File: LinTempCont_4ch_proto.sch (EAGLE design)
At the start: 76 parts, among them IC1 LM393D, IC3 AD5624R, IC4 AD5262, T1 MMBT3904, T2 MMBT3904, X1 BNC-H, X2 BNC-H

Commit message: Main board progress, started individual channel boards
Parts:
- removed RI, RP: DNP, rlc-jqi:RES0805
- added C16, C17, C18, C19: 10nF, rcl:C-EUC0603
- added C20, C22, C24: 100nF, rlc-jqi:CAP0603
- added C21, C23, C25: 10uF, rlc-jqi:CAP0603
- added D2, D3, D4: (no value), Lin-Temp-Controller:LED/MINI-IND
- added ENC1, ENC2: PEC09, connector-jqi:PEC09
- added IC10, IC5, IC8: AD5262, Lin-Temp-Controller:AD5262
- added IC2, IC7, IC9: LM393D, Lin-Temp-Controller:LM393D
- added JP10, JP12, JP13, JP6, JP7, JP9: (no value), pinhead:PINHD-1X2
- added JP11, JP2, JP8: (no value), pinhead:PINHD-2X6/90
- added R19, R28, R29, R32, R33, R34, R43, R44, R45, R47, R48, R61, R62, R63, R65, R66, R79, R80, R81, R83, R84: 10k, rlc-jqi:RES0603
- added R30, R31, R36: 50, rlc-jqi:RES0603
- added R35: 50, rlc-jqi:RES0805
- added R37, R39, R55, R57, R73, R75: 4.3k, rlc-jqi:RES0603
- added R38, R40, R56, R58, R74, R76: 1.5k, rlc-jqi:RES0603
- added R41, R42, R59, R60, R77, R78: 10k, Lin-Temp-Controller:MODEL64_TRIMPOT/TOP-ADJ
- added R46, R64, R82: 33k, rlc-jqi:RES0603
- added R49, R67, R85: 330, rlc-jqi:RES0603
- added R50, R51, R68, R69, R86, R87: 0, rlc-jqi:RES0603
- added R52, R53, R54, R70, R71, R72, R88, R89, R90: 1.0k, rlc-jqi:RES0603
- added RI1, RI2, RI3, RP1, RP2, RP3: DNP, rlc-jqi:RES0603
- added S2, S3, S4: (no value), Lin-Temp-Controller:SWITCH-DPDT/VER
- added T3, T4, T5, T6, T7, T8: MMBT3904, Lin-Temp-Controller:MMBT3904
- added TP10, TP11, TP12, TP13, TP14, TP15, TP16, TP17, TP18, TP19, TP20, TP21, TP22, TP23, TP24, TP25, TP26, TP9: TESTPT, Lin-Temp-Controller:TESTPT
- added X3, X4, X5, X6, X7, X8: BNC-H, connector-jqi:BNC-H
- C1, C10, C11, C12, C13, C14, C15, C2, C27, C3, C30, C4, C5, C6, C7, C8, C9: device rlc-jqi:CAP0805 -> rlc-jqi:CAP0603
- D1: device Lin-Temp-Controller:LED -> Lin-Temp-Controller:LED/MINI-IND
- L2: device rlc-jqi:INDUCTOR-0805 -> rlc-jqi:INDUCTOR-0603
- R1, R10, R11, R12, R13, R14, R15, R16, R17, R18, R2, R3, R4, R8, R9: device rlc-jqi:RES0805 -> rlc-jqi:RES0603
- R20, R21, R22, R23, R24, R25, R26, R27: device jqi_passives:R_SMDR0805 -> jqi_passives:R_SMDR0603
- R5: value 300 -> 330; device rlc-jqi:RES0805 -> rlc-jqi:RES0603
- S1: device Lin-Temp-Controller:SWITCH-DPDT -> Lin-Temp-Controller:SWITCH-DPDT/VER
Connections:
- net LIMA renamed LIMA1
- net LIMB renamed LIMB1
- removed net +1V: JP1.11, R16.P$2, R17.P$1, RI.P$2, RP.P$1, TP5.P$1
- removed net I: IC4.A2, JP1.12, RI.P$1, TP6.P$1
- removed net N$99: U$1.21/A7/PWM
- removed net P: IC4.A1, JP1.9, RP.P$2, TP4.P$1
- new net +1V_1: JP1.11, R16.P$2, R17.P$1, TP5.P$1
- new net +1V_2: JP2.11, R50.P$2, R51.P$1, RI1.P$2, RP1.P$1, TP12.P$1
- new net +1V_3: JP8.11, R68.P$2, R69.P$1, RI2.P$2, RP2.P$1, TP18.P$1
- new net +1V_4: JP11.11, R86.P$2, R87.P$1, RI3.P$2, RP3.P$1, TP24.P$1
- new net ENC_SW2: ENC2.E, R34.P$1, U$1.21/A7/PWM
- new net I1: IC4.A2, JP1.12, TP6.P$1
- new net I2: IC5.A2, JP2.12, RI1.P$1, TP13.P$1
- new net I3: IC8.A2, JP8.12, RI2.P$1, TP19.P$1
- new net I4: IC10.A2, JP11.12, RI3.P$1, TP25.P$1
- new net LIMA2: JP2.5, R38.P$2, T3.C
- new net LIMA3: JP8.5, R56.P$2, T5.C
- new net LIMA4: JP11.5, R74.P$2, T7.C
- new net LIMB2: JP2.7, R40.P$2, T4.C
- new net LIMB3: JP8.7, R58.P$2, T6.C
- new net LIMB4: JP11.7, R76.P$2, T8.C
- new net N$15: ENC1.GND, R30.P$2
- new net N$16: ENC1.D, R31.P$2
- new net N$17: ENC2.GND, R35.P$2
- new net N$19: ENC2.D, R36.P$2
- new net N$21: JP6.1, R37.P$2, R38.P$1, S2.3
- new net N$22: JP7.1, R39.P$2, R40.P$1, S2.6
- new net N$23: IC2A.-IN, R41.1, R43.P$1, TP9.P$1
- new net N$26: IC2A.OUT, R44.P$1, R45.P$2
- new net N$27: R45.P$1, T3.B
- new net N$28: IC2B.+IN, R42.1, R46.P$1, TP10.P$1
- new net N$29: IC2B.OUT, R47.P$1, R48.P$2
- new net N$30: R48.P$1, T4.B
- new net N$31: D2.C, R49.P$2
- new net N$32: R49.P$1, S2.4
- new net N$33: IC5.B1, IC5.W1, R50.P$1
- new net N$34: IC5.B2, IC5.W2, R51.P$2
- new net N$35: JP2.6, R52.P$1, R53.P$1
- new net N$36: R52.P$2, X3.1
- new net N$37: R54.P$2, X4.1
- new net N$38: JP9.1, R55.P$2, R56.P$1, S3.3
- new net N$39: JP10.1, R57.P$2, R58.P$1, S3.6
- new net N$40: IC7A.-IN, R59.1, R61.P$1, TP15.P$1
- new net N$41: IC7A.OUT, R62.P$1, R63.P$2
- new net N$42: R63.P$1, T5.B
- new net N$43: IC7B.+IN, R60.1, R64.P$1, TP16.P$1
- new net N$44: IC7B.OUT, R65.P$1, R66.P$2
- new net N$45: R66.P$1, T6.B
- new net N$46: D3.C, R67.P$2
- new net N$47: R67.P$1, S3.4
- new net N$48: IC8.B1, IC8.W1, R68.P$1
- new net N$49: IC8.B2, IC8.W2, R69.P$2
- new net N$50: JP8.6, R70.P$1, R71.P$1
- new net N$51: R70.P$2, X5.1
- new net N$52: R72.P$2, X6.1
- new net N$53: JP12.1, R73.P$2, R74.P$1, S4.3
- new net N$54: JP13.1, R75.P$2, R76.P$1, S4.6
- new net N$55: IC9A.-IN, R77.1, R79.P$1, TP21.P$1
- new net N$56: IC9A.OUT, R80.P$1, R81.P$2
- new net N$57: R81.P$1, T7.B
- new net N$58: IC9B.+IN, R78.1, R82.P$1, TP22.P$1
- new net N$59: IC9B.OUT, R83.P$1, R84.P$2
- new net N$60: R84.P$1, T8.B
- new net N$61: D4.C, R85.P$2
- new net N$62: R85.P$1, S4.4
- new net N$63: IC10.B1, IC10.W1, R86.P$1
- new net N$64: IC10.B2, IC10.W2, R87.P$2
- new net N$65: JP11.6, R88.P$1, R89.P$1
- new net N$66: R88.P$2, X7.1
- new net N$67: R90.P$2, X8.1
- new net P1: IC4.A1, JP1.9, TP4.P$1
- new net P2: IC5.A1, JP2.9, RP1.P$2, TP11.P$1
- new net P3: IC8.A1, JP8.9, RP2.P$2, TP17.P$1
- new net P4: IC10.A1, JP11.9, RP3.P$2, TP23.P$1
- net 2.5V: now also JP11.10, JP2.10, JP8.10
- net ACT_T2: now also R53.P$2
- net ACT_T3: now also R71.P$2
- net ACT_T4: now also R89.P$2
- net AGND: now also C20.P$1, C21.P$1, C22.P$1, C23.P$1, C24.P$1, C25.P$1, IC10.GND, IC2P.V-, IC5.GND, IC7P.V-, IC8.GND, IC9P.V-, JP10.2, JP11.2, JP12.2, JP13.2, JP2.2, JP6.2, JP7.2, JP8.2, JP9.2, R37.P$1, R39.P$1, R41.2, R41.3, R42.2, R42.3, R55.P$1, R57.P$1, R59.2, R59.3, R60.2, R60.3, R73.P$1, R75.P$1, R77.2, R77.3, R78.2, R78.3, S2.2, S2.5, S3.2, S3.5, S4.2, S4.5, T3.E, T4.E, T5.E, T6.E, T7.E, T8.E, X3.2, X4.2, X5.2, X6.2, X7.2, X8.2
- net CS_POT2: now also IC5.CS
- net CS_POT3: now also IC8.CS
- net CS_POT4: now also IC10.CS
- net DGND: now also C16.1, C17.1, C18.1, C19.1, IC10.VSS, IC5.VSS, IC8.VSS, R30.P$1, R31.P$1, R35.P$1, R36.P$1
- net ENC_A1: now also C17.2, ENC1.A, R28.P$1
- net ENC_A2: now also C19.2, ENC2.A, R33.P$1
- net ENC_B1: now also C16.2, ENC1.B, R19.P$1
- net ENC_B2: now also C18.2, ENC2.B, R32.P$1
- net ENC_SW1: now also ENC1.E, R29.P$1
- net MOSI_B: now also IC10.SDI, IC5.SDI, IC8.SDI
- net SCK_B: now also IC10.CLK, IC5.CLK, IC8.CLK
- net VDD: now also C20.P$2, C21.P$2, C22.P$2, C23.P$2, C24.P$2, C25.P$2, D2.A, D3.A, D4.A, IC10.PR, IC10.SHDN, IC10.VDD, IC10.VL, IC2P.V+, IC5.PR, IC5.SHDN, IC5.VDD, IC5.VL, IC7P.V+, IC8.PR, IC8.SHDN, IC8.VDD, IC8.VL, IC9P.V+, JP11.1, JP2.1, JP8.1, R19.P$2, R28.P$2, R29.P$2, R32.P$2, R33.P$2, R34.P$2, R43.P$2, R44.P$2, R46.P$2, R47.P$2, R61.P$2, R62.P$2, R64.P$2, R65.P$2, R79.P$2, R80.P$2, R82.P$2, R83.P$2
- net VMON2: now also JP2.8, R54.P$1
- net VMON3: now also JP8.8, R72.P$1
- net VMON4: now also JP11.8, R90.P$1
- net VSET2: now also IC2A.+IN, IC2B.-IN, JP2.3, TP14.P$1
- net VSET3: now also IC7A.+IN, IC7B.-IN, JP8.3, TP20.P$1
- net VSET4: now also IC9A.+IN, IC9B.-IN, JP11.3, TP26.P$1

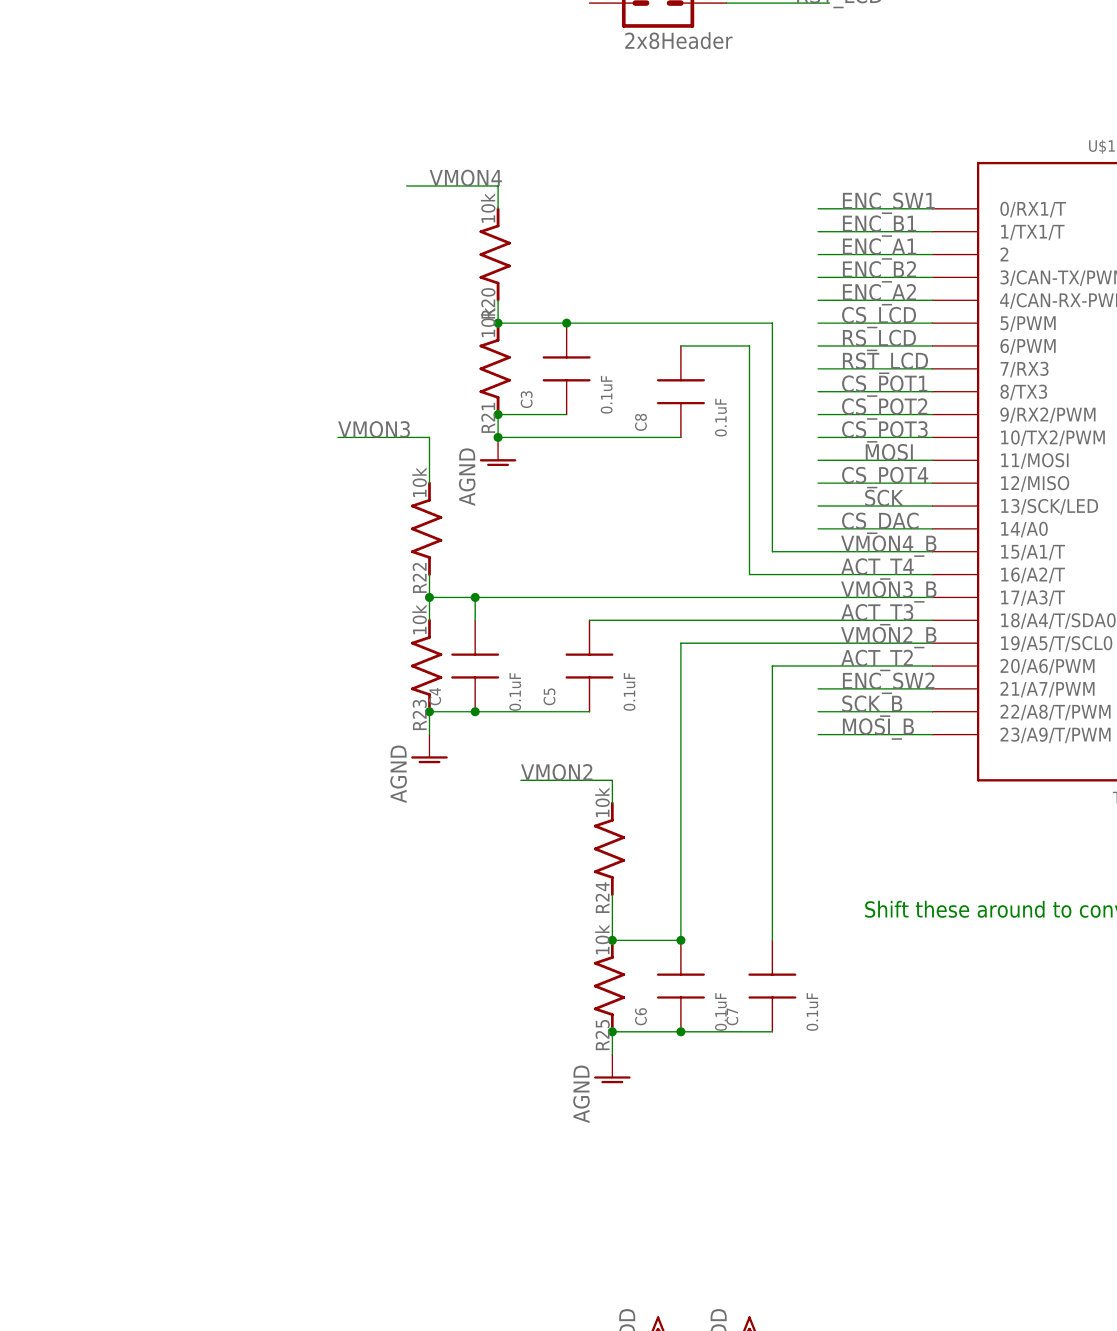
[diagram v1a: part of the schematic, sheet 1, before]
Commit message: Schematic updates and progress routing both boards
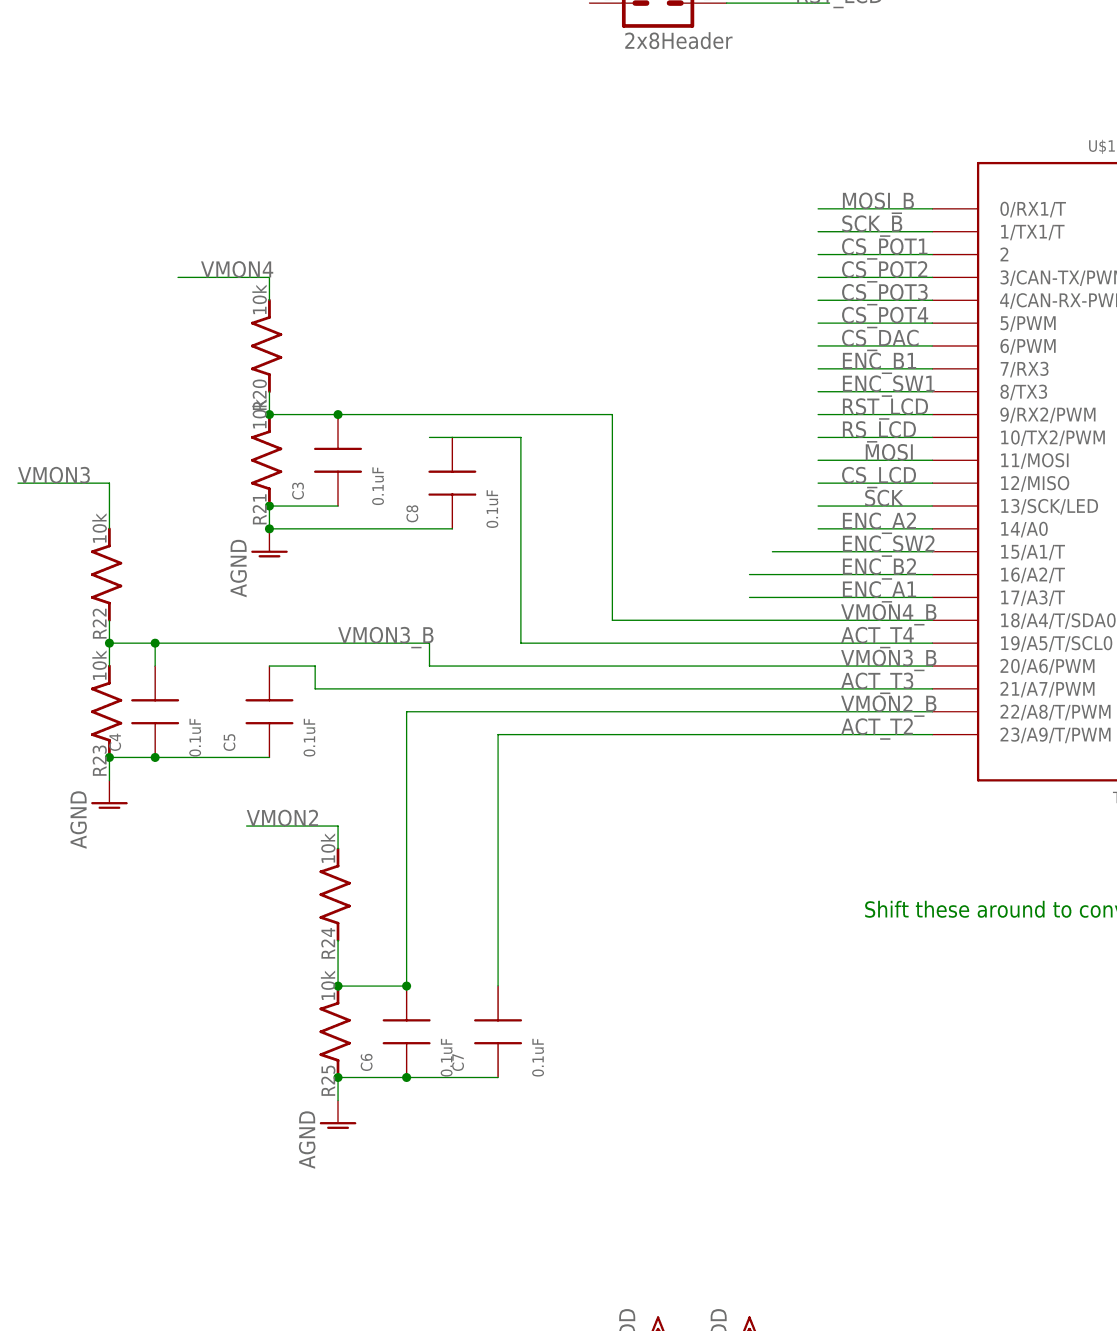
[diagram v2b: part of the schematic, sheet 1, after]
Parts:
- removed R16, R17, R50, R51, R68, R69, R86, R87: 0, rlc-jqi:RES0603
- removed RI1, RI2, RI3, RP1, RP2, RP3: DNP, rlc-jqi:RES0603
- R35: device rlc-jqi:RES0805 -> rlc-jqi:RES0603
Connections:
- removed net N$18: IC4.B1, IC4.W1, R16.P$1
- removed net N$2: JP1.6, R14.P$1, R15.P$1
- removed net N$20: IC4.B2, IC4.W2, R17.P$2
- removed net N$33: IC5.B1, IC5.W1, R50.P$1
- removed net N$34: IC5.B2, IC5.W2, R51.P$2
- removed net N$48: IC8.B1, IC8.W1, R68.P$1
- removed net N$49: IC8.B2, IC8.W2, R69.P$2
- removed net N$63: IC10.B1, IC10.W1, R86.P$1
- removed net N$64: IC10.B2, IC10.W2, R87.P$2
- new net N$69: JP1.8, R14.P$1, R15.P$1
- net +1V_1: now also IC4.B1, IC4.B2, IC4.W1, IC4.W2, JP1.3; no longer JP1.11, R16.P$2, R17.P$1
- net +1V_2: now also IC5.B1, IC5.B2, IC5.W1, IC5.W2, JP2.3; no longer JP2.11, R50.P$2, R51.P$1, RI1.P$2, RP1.P$1
- net +1V_3: now also IC8.B1, IC8.B2, IC8.W1, IC8.W2, JP8.3; no longer JP8.11, R68.P$2, R69.P$1, RI2.P$2, RP2.P$1
- net +1V_4: now also IC10.B1, IC10.B2, IC10.W1, IC10.W2, JP11.3; no longer JP11.11, R86.P$2, R87.P$1, RI3.P$2, RP3.P$1
- net 2.5V: now also JP1.9, JP11.9, JP2.9, JP8.9; no longer JP1.10, JP11.10, JP2.10, JP8.10
- net ACT_T2: now also U$1.23/A9/T/PWM; no longer U$1.20/A6/PWM
- net ACT_T3: now also U$1.21/A7/PWM; no longer U$1.18/A4/T/SDA0
- net ACT_T4: now also U$1.19/A5/T/SCL0; no longer U$1.16/A2/T
- net AGND: now also JP1.12, JP11.12, JP2.12, JP8.12; no longer JP1.2, JP11.2, JP2.2, JP8.2
- net CS_DAC: now also U$1.6/PWM; no longer U$1.14/A0
- net CS_LCD: now also U$1.12/MISO; no longer U$1.5/PWM
- net CS_POT1: now also U$1.2; no longer U$1.8/TX3
- net CS_POT2: now also U$1.3/CAN-TX/PWM; no longer U$1.9/RX2/PWM
- net CS_POT3: now also U$1.4/CAN-RX-PWM; no longer U$1.10/TX2/PWM
- net CS_POT4: now also U$1.5/PWM; no longer U$1.12/MISO
- net ENC_A1: now also U$1.17/A3/T; no longer U$1.2
- net ENC_A2: now also U$1.14/A0; no longer U$1.4/CAN-RX-PWM
- net ENC_B1: now also U$1.7/RX3; no longer U$1.1/TX1/T
- net ENC_B2: now also U$1.16/A2/T; no longer U$1.3/CAN-TX/PWM
- net ENC_SW1: now also U$1.8/TX3; no longer U$1.0/RX1/T
- net ENC_SW2: now also U$1.15/A1/T; no longer U$1.21/A7/PWM
- net I1: now also JP1.5; no longer JP1.12
- net I2: now also JP2.5; no longer JP2.12, RI1.P$1
- net I3: now also JP8.5; no longer JP8.12, RI2.P$1
- net I4: now also JP11.5; no longer JP11.12, RI3.P$1
- net LIMA1: now also JP1.4; no longer JP1.5
- net LIMA2: now also JP2.4; no longer JP2.5
- net LIMA3: now also JP8.4; no longer JP8.5
- net LIMA4: now also JP11.4; no longer JP11.5
- net LIMB1: now also JP1.6; no longer JP1.7
- net LIMB2: now also JP2.6; no longer JP2.7
- net LIMB3: now also JP8.6; no longer JP8.7
- net LIMB4: now also JP11.6; no longer JP11.7
- net MOSI_B: now also U$1.0/RX1/T; no longer U$1.23/A9/T/PWM
- net N$35: now also JP2.8; no longer JP2.6
- net N$50: now also JP8.8; no longer JP8.6
- net N$65: now also JP11.8; no longer JP11.6
- net P1: now also JP1.1; no longer JP1.9
- net P2: now also JP2.1; no longer JP2.9, RP1.P$2
- net P3: now also JP8.1; no longer JP8.9, RP2.P$2
- net P4: now also JP11.1; no longer JP11.9, RP3.P$2
- net RST_LCD: now also U$1.9/RX2/PWM; no longer U$1.7/RX3
- net RS_LCD: now also U$1.10/TX2/PWM; no longer U$1.6/PWM
- net SCK_B: now also U$1.1/TX1/T; no longer U$1.22/A8/T/PWM
- net VDD: now also JP1.11, JP1.2, JP11.11, JP11.2, JP2.11, JP2.2, JP8.11, JP8.2; no longer JP1.1, JP11.1, JP2.1, JP8.1
- net VMON1: now also JP1.7; no longer JP1.8
- net VMON2: now also JP2.7; no longer JP2.8
- net VMON2_B: now also U$1.22/A8/T/PWM; no longer U$1.19/A5/T/SCL0
- net VMON3: now also JP8.7; no longer JP8.8
- net VMON3_B: now also U$1.20/A6/PWM; no longer U$1.17/A3/T
- net VMON4: now also JP11.7; no longer JP11.8
- net VMON4_B: now also U$1.18/A4/T/SDA0; no longer U$1.15/A1/T
- net VSET1: now also JP1.10; no longer JP1.3
- net VSET2: now also JP2.10; no longer JP2.3
- net VSET3: now also JP8.10; no longer JP8.3
- net VSET4: now also JP11.10; no longer JP11.3
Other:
- note removed: "If there's room, consider BNC for set temp"
- moved on the sheet: C3, C4, C5, C6, C7, C8, R20, R21, R22, R23, R24, R25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

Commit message: Board/Schematic updates and tweaks
Incorporate suggestions from Neal and Alessandro
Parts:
- L2: device rlc-jqi:INDUCTOR-0603 -> rlc-jqi:INDUCTOR-0805
- R28, R33: device rlc-jqi:RES0603 -> jqi_passives:R_SMDR0603
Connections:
- net ENC_A1: now also R28.1; no longer R28.P$1
- net ENC_A2: now also R33.1; no longer R33.P$1
- net VDD: now also R28.2, R33.2; no longer R28.P$2, R33.P$2
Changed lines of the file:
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@@
 <part name="VDD11" library="supply1" deviceset="VDD" device=""/>
 <part name="U$1" library="mcu-accessories" deviceset="TEENSY_3.1+4" device=""/>
-<part name="L2" library="rlc-jqi" deviceset="INDUCTOR" device="-0603" value="Ferrite 1k"/>
+<part name="L2" library="rlc-jqi" deviceset="INDUCTOR" device="-0805" value="Ferrite 1k"/>
 <part name="AGND20" library="supply1" deviceset="AGND" device=""/>
 <part name="R20" library="jqi_passives" deviceset="R_SMD" device="R0603" value="10k"/>
@@
 <part name="ENC1" library="connector-jqi" deviceset="PEC09" device=""/>
 <part name="R19" library="rlc-jqi" deviceset="RES" device="0603" value="10k"/>
-<part name="R28" library="rlc-jqi" deviceset="RES" device="0603" value="10k"/>
+<part name="R28" library="jqi_passives" deviceset="R_SMD" device="R0603" value="10k"/>
 <part name="R29" library="rlc-jqi" deviceset="RES" device="0603" value="10k"/>
 <part name="C16" library="rcl" deviceset="C-EU" device="C0603" value="10nF"/>
@@
 <part name="ENC2" library="connector-jqi" deviceset="PEC09" device=""/>
 <part name="R32" library="rlc-jqi" deviceset="RES" device="0603" value="10k"/>
-<part name="R33" library="rlc-jqi" deviceset="RES" device="0603" value="10k"/>
+<part name="R33" library="jqi_passives" deviceset="R_SMD" device="R0603" value="10k"/>
 <part name="R34" library="rlc-jqi" deviceset="RES" device="0603" value="10k"/>
 <part name="C18" library="rcl" deviceset="C-EU" device="C0603" value="10nF"/>
@@
 <segment>
 <wire x1="68.58" y1="-77.47" x2="68.58" y2="-76.2" width="0.1524" layer="91"/>
-<pinref part="R28" gate="G$1" pin="P$2"/>
+<pinref part="R28" gate="G$1" pin="2"/>
 <pinref part="VDD12" gate="G$1" pin="VDD"/>
 <wire x1="68.58" y1="-76.2" x2="68.58" y2="-82.55" width="0.1524" layer="91"/>
@@
 <segment>
 <wire x1="180.34" y1="-77.47" x2="180.34" y2="-76.2" width="0.1524" layer="91"/>
-<pinref part="R33" gate="G$1" pin="P$2"/>
+<pinref part="R33" gate="G$1" pin="2"/>
 <pinref part="VDD16" gate="G$1" pin="VDD"/>
 <wire x1="180.34" y1="-76.2" x2="180.34" y2="-82.55" width="0.1524" layer="91"/>
@@
 <net name="ENC_A2" class="0">
 <segment>
-<pinref part="R33" gate="G$1" pin="P$1"/>
+<pinref part="R33" gate="G$1" pin="1"/>
 <wire x1="180.34" y1="-92.71" x2="180.34" y2="-95.25" width="0.1524" layer="91"/>
 <pinref part="ENC2" gate="G$1" pin="A"/>
@@
 <net name="ENC_A1" class="0">
 <segment>
-<pinref part="R28" gate="G$1" pin="P$1"/>
+<pinref part="R28" gate="G$1" pin="1"/>
 <wire x1="68.58" y1="-92.71" x2="68.58" y2="-95.25" width="0.1524" layer="91"/>
 <pinref part="ENC1" gate="G$1" pin="A"/>

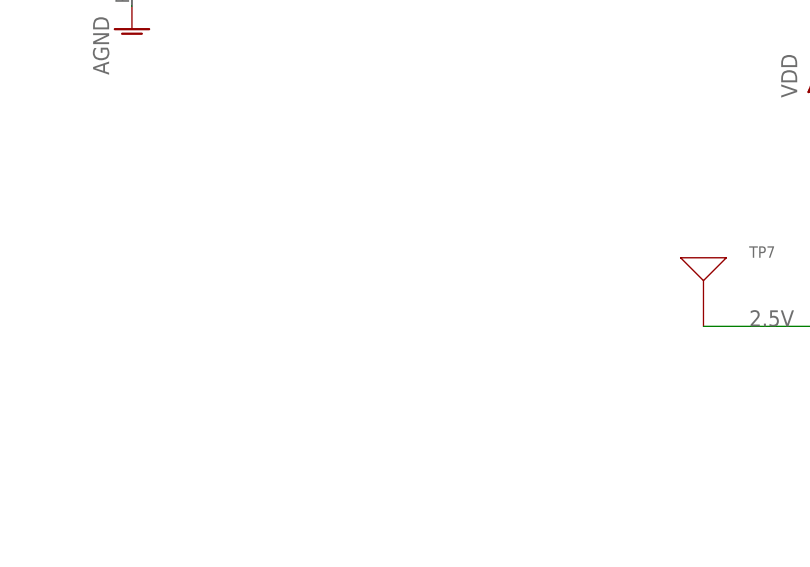
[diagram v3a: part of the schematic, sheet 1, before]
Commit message: Board/Schematic Clean up-lcd.init tweak
Added encoder hold event to initialize LCD to try to get around bug
where LCD display goes blank. The bug appears to be from a loose solder
connection on first prototype
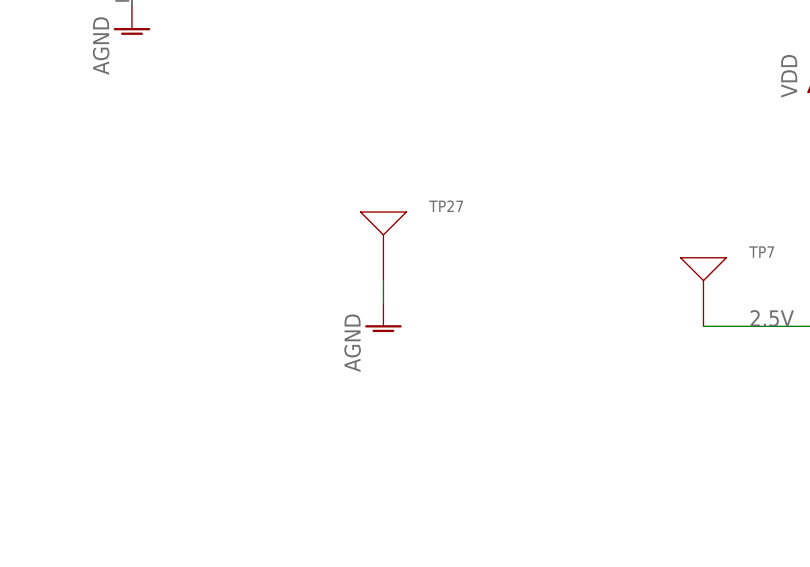
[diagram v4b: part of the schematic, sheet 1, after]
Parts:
- added TP27: TESTPT, Lin-Temp-Controller:TESTPT
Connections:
- net AGND: now also TP27.P$1
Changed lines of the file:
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@@
 <part name="VDD42" library="supply1" deviceset="VDD" device=""/>
 <part name="AGND42" library="supply1" deviceset="AGND" device=""/>
+<part name="TP27" library="Lin-Temp-Controller" deviceset="TESTPT" device=""/>
+<part name="AGND43" library="supply1" deviceset="AGND" device=""/>
 </parts>
 <sheets>
@@
 <instance part="JP4" gate="G$1" x="233.68" y="93.98" rot="R180"/>
 <instance part="L5" gate="G$1" x="304.8" y="99.06" rot="R180"/>
+<instance part="TP27" gate="G$1" x="193.04" y="-27.94"/>
+<instance part="AGND43" gate="VR1" x="193.04" y="-35.56"/>
 </instances>
 <busses>
@@
 <wire x1="236.22" y1="91.44" x2="254" y2="91.44" width="0.1524" layer="91"/>
 </segment>
+<segment>
+<pinref part="TP27" gate="G$1" pin="P$1"/>
+<pinref part="AGND43" gate="VR1" pin="AGND"/>
+<wire x1="193.04" y1="-30.48" x2="193.04" y2="-33.02" width="0.1524" layer="91"/>
+</segment>
 </net>
